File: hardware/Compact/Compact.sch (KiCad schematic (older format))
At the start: 55 parts, among them J2 Battery, J3 GPIO, J4 USB_B_Micro, J6 LEDs, J7 GPIO, Q1 BSS806N, Q2 BSS806N, Q3 BSS806N, Q4 BSS806N, SW1 Mode, SW2 Power, U1 STM32F411CE, U2 AP2210N-3.3TRG1, U3 MCP73831T-2ACI_OT, U5 GD25Q16CEIGR, Y1 24Mhz

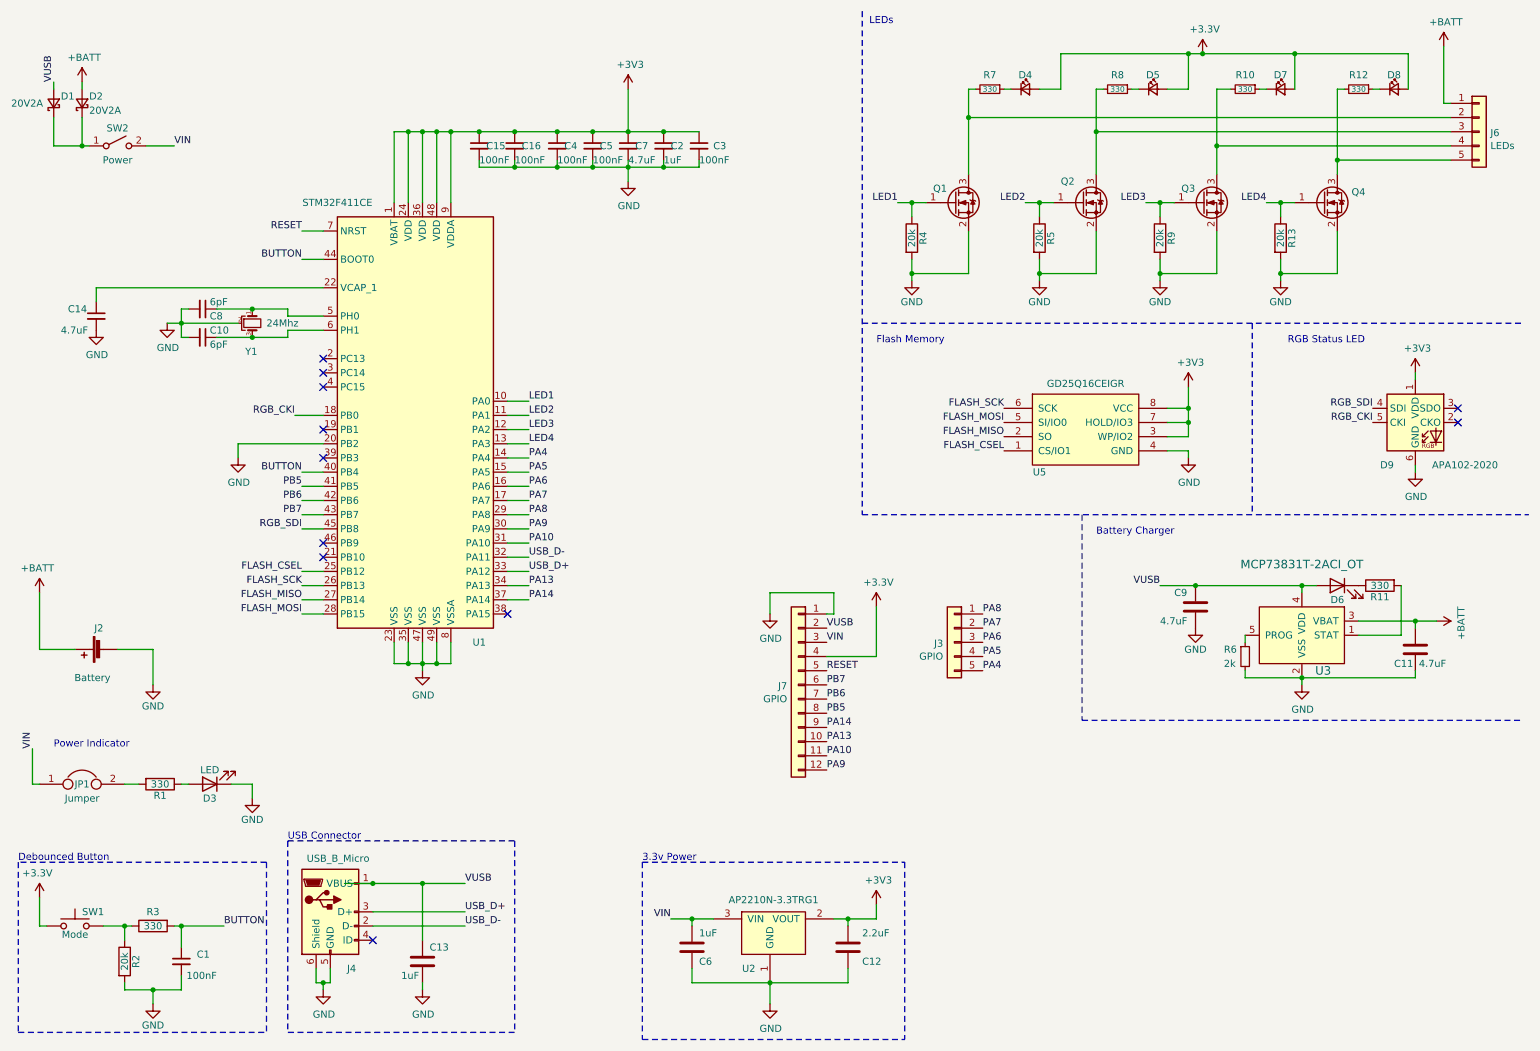
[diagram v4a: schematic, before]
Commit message: Add ESD. Update labeling
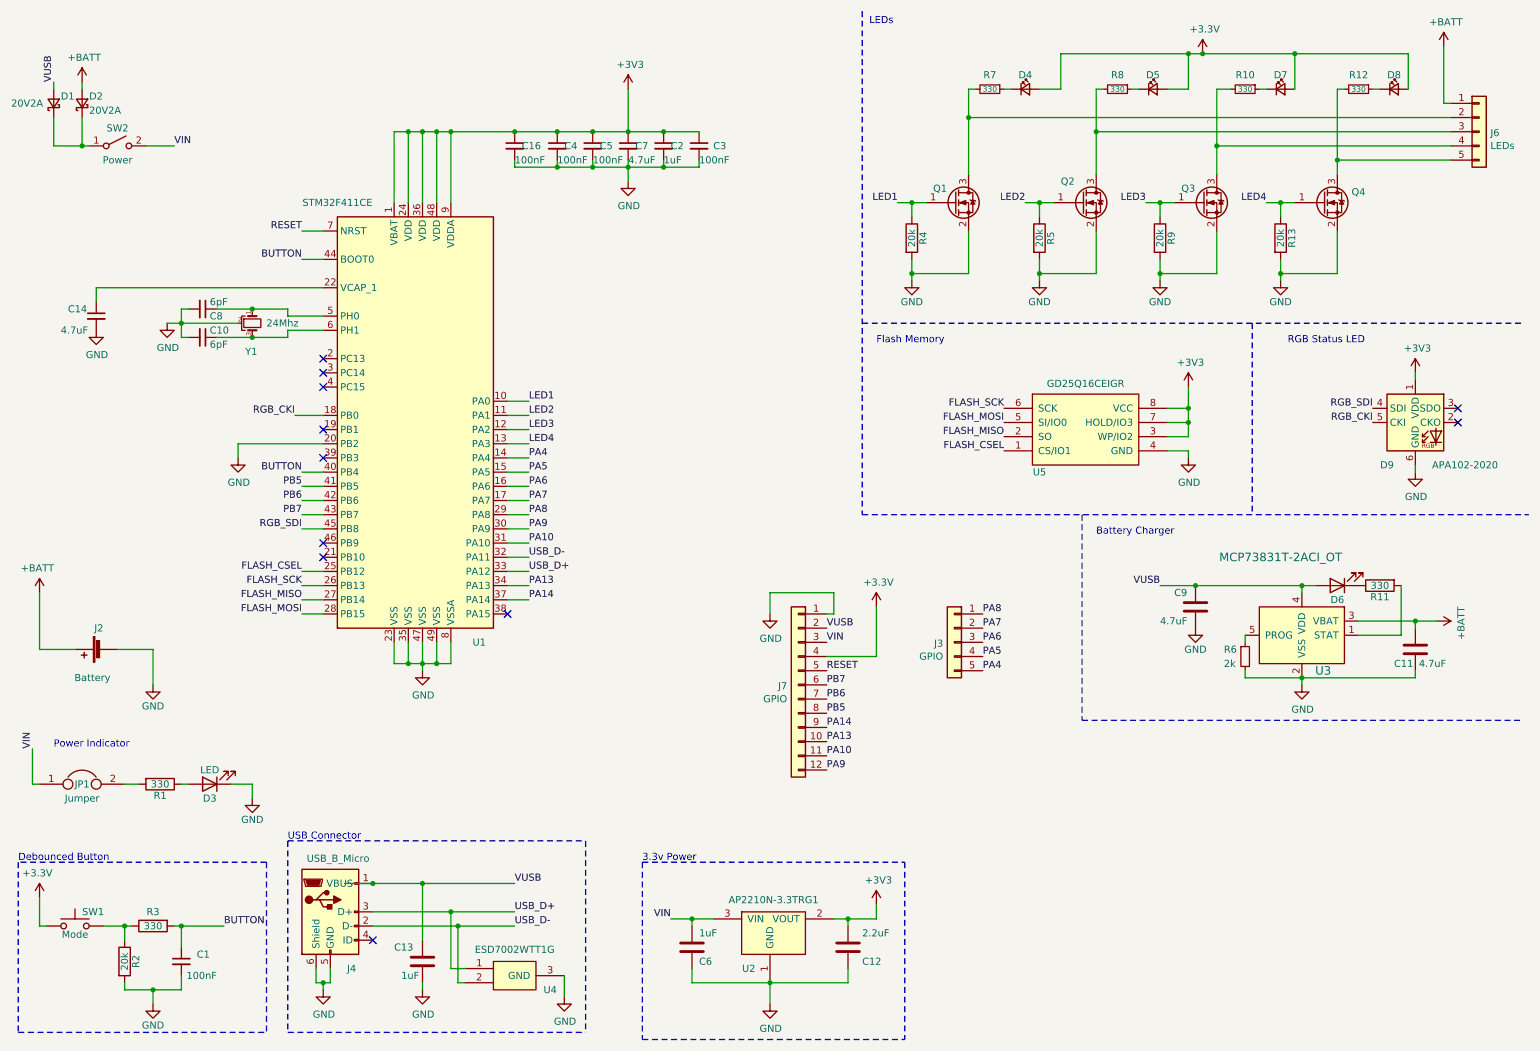
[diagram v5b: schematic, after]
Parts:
- removed C15: 100nF, Capacitor_SMD:C_0603_1608Metric, symbol Device:C_Small
- added U4: ESD7002WTT1G, Package_TO_SOT_SMD:SOT-323_SC-70, symbol Project:ESD7002WTT1G
- D3: MPN 150060SS75000 -> 150060BS55040
- D6: MPN 150060BS55040 -> 150060SS75000
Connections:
- net GND: now also U4.3 (GND)
- net USB_D+: now also U4.1
- net USB_D-: now also U4.2
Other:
- moved on the sheet: D6
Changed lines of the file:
@@
 	1    0    0    -1
 $EndComp
-Connection ~ 3850 1350
 Wire Wire Line
 	3550 1350 3650 1350
-Wire Wire Line
-	3850 1350 4100 1350
 Connection ~ 4100 1350
 Wire Wire Line
-	3850 1550 3850 1600
-Wire Wire Line
-	3850 1600 4100 1600
-Wire Wire Line
 	4100 1550 4100 1600
-Connection ~ 4100 1600
 Connection ~ 4400 1350
 Wire Wire Line
@@
 U 1 1 5DAA61BD
 P 3450 7200
-F 0 "C13" H 3500 7100 50  0000 L CNN
+F 0 "C13" H 3250 7100 50  0000 L CNN
 F 1 "1uF" H 3300 7300 50  0000 L CNN
 F 2 "Capacitor_SMD:C_0603_1608Metric" H 3488 7050 50  0001 C CNN
@@
 Wire Wire Line
 	2150 2700 1750 2700
-$Comp
-L Device:C_Small C15
-U 1 1 5E4C30F8
-P 3850 1450
-F 0 "C15" H 3900 1450 50  0000 L CNN
-F 1 "100nF" H 3850 1350 50  0000 L CNN
-F 2 "Capacitor_SMD:C_0603_1608Metric" H 3850 1450 50  0001 C CNN
-F 3 "~" H 3850 1450 50  0001 C CNN
-F 4 "AVX" H 3850 1450 50  0001 C CNN "MFN"
-F 5 "06035C104K4T2A" H 3850 1450 50  0001 C CNN "MPN"
-F 6 "0603" H -500 -250 50  0001 C CNN "Package"
-	1    3850 1450
-	1    0    0    -1
-$EndComp
 NoConn ~ 3100 7050
 $Comp
@@
 F 2 "LED_SMD:LED_0603_1608Metric_Castellated" H 1950 5950 50  0001 C CNN
 F 3 "" H 1950 5950 50  0001 C CNN
-F 4 "150060SS75000" H 1950 5950 50  0001 C CNN "MPN"
+F 4 "150060BS55040" H 1950 5950 50  0001 C CNN "MPN"
 F 5 "0603" H 600 1700 50  0001 C CNN "Package"
 	1    1950 5950
@@
 $EndComp
 $Comp
-L Device:LED D?
-U 1 1 5F01DF05
-P 9900 4550
-AR Path="/5BD64BD8/5F01DF05" Ref="D?"  Part="1"
-AR Path="/5F01DF05" Ref="D6"  Part="1"
-F 0 "D6" H 9900 4450 50  0000 C CNN
-F 1 "LED" H 9900 4450 50  0001 C CNN
-F 2 "LED_SMD:LED_0603_1608Metric" H 9900 4550 50  0001 C CNN
-F 3 "" H 9900 4550 50  0001 C CNN
-F 4 "150060BS55040" H 9900 4550 50  0001 C CNN "MPN"
-F 5 "0603" H 800 -300 50  0001 C CNN "Package"
-	1    9900 4550
-	-1   0    0    -1
-$EndComp
-$Comp
 L Device:R R?
 U 1 1 5F01DF0D
@@
 P 9650 4800
 F 0 "U3" H 9800 4450 60  0000 C CNN
-F 1 "MCP73831T-2ACI_OT" H 9650 5200 60  0000 C CNN
+F 1 "MCP73831T-2ACI_OT" H 9500 5250 60  0000 C CNN
 F 2 "Package_TO_SOT_SMD:SOT-23-5" H 9850 5000 60  0001 L CNN
 F 3 "http://ww1.microchip.com/downloads/en/DeviceDoc/20001984g.pdf" H 9850 5100 60  0001 L CNN
@@
 	3650 1350 3650 1850
 Connection ~ 3650 1350
-Wire Wire Line
-	3650 1350 3850 1350
 Wire Wire Line
 	5900 4750 5900 4600
@@
 Wire Wire Line
 	2900 6650 3100 6650
-Text Label 3750 6650 0    50   ~ 0
+Text Label 4100 6650 0    50   ~ 0
 VUSB
-Text Label 3750 6950 0    50   ~ 0
+Text Label 4100 6950 0    50   ~ 0
 USB_D-
-Text Label 3750 6850 0    50   ~ 0
+Text Label 4100 6850 0    50   ~ 0
 USB_D+
 Connection ~ 3100 6650
-Wire Wire Line
-	3100 6850 3750 6850
-Wire Wire Line
-	3100 6950 3750 6950
-Wire Wire Line
-	3450 6650 3750 6650
-Wire Notes Line
-	2500 6350 4100 6350
-Wire Notes Line
-	4100 6350 4100 7700
-Wire Notes Line
-	4100 7700 2500 7700
 $Comp
 L Device:Jumper JP1
@@
 	0    1    1    0
 $EndComp
+$Comp
+L Project:ESD7002WTT1G U4
+U 1 1 5FC059CD
+P 4100 7300
+F 0 "U4" H 4350 7200 50  0000 C CNN
+F 1 "ESD7002WTT1G" H 4100 7484 50  0000 C CNN
+F 2 "Package_TO_SOT_SMD:SOT-323_SC-70" H 4100 7600 50  0001 C CNN
+F 3 "https://www.onsemi.com/pub/Collateral/ESD7002-D.PDF" H 3950 7400 50  0001 C CNN
+	1    4100 7300
+	1    0    0    -1
+$EndComp
+$Comp
+L power:GND #PWR06
+U 1 1 5FC07465
+P 4450 7450
+F 0 "#PWR06" H 4450 7200 50  0001 C CNN
+F 1 "GND" H 4455 7277 50  0000 C CNN
+F 2 "" H 4450 7450 50  0001 C CNN
+F 3 "" H 4450 7450 50  0001 C CNN
+	1    4450 7450
+	1    0    0    -1
+$EndComp
+Wire Wire Line
+	4450 7450 4450 7300
+Wire Wire Line
+	3100 6950 3700 6950
+Wire Wire Line
+	3100 6850 3650 6850
+Wire Wire Line
+	3750 7350 3700 7350
+Wire Wire Line
+	3700 7350 3700 6950
+Connection ~ 3700 6950
+Wire Wire Line
+	3750 7250 3650 7250
+Wire Wire Line
+	3650 7250 3650 6850
+Connection ~ 3650 6850
+Wire Wire Line
+	3450 6650 4100 6650
+Wire Wire Line
+	3650 6850 4100 6850
+Wire Wire Line
+	3700 6950 4100 6950
+Wire Notes Line
+	2500 6350 4600 6350
+Wire Notes Line
+	2500 7700 4600 7700
+Wire Notes Line
+	4600 6350 4600 7700
+Wire Wire Line
+	3650 1350 4100 1350
+$Comp
+L Device:LED D?
+U 1 1 5F01DF05
+P 9900 4550
+AR Path="/5BD64BD8/5F01DF05" Ref="D?"  Part="1"
+AR Path="/5F01DF05" Ref="D6"  Part="1"
+F 0 "D6" H 9900 4650 50  0000 C CNN
+F 1 "LED" H 9900 4450 50  0001 C CNN
+F 2 "LED_SMD:LED_0603_1608Metric" H 9900 4550 50  0001 C CNN
+F 3 "" H 9900 4550 50  0001 C CNN
+F 4 "150060SS75000" H 9900 4550 50  0001 C CNN "MPN"
+F 5 "0603" H 800 -300 50  0001 C CNN "Package"
+	1    9900 4550
+	-1   0    0    1
+$EndComp
 $EndSCHEMATC
